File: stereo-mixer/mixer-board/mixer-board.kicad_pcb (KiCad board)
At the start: 2 copper layers, 26 parts, among them J1 Conn_01x36_Male, J2 Conn_01x03_Male

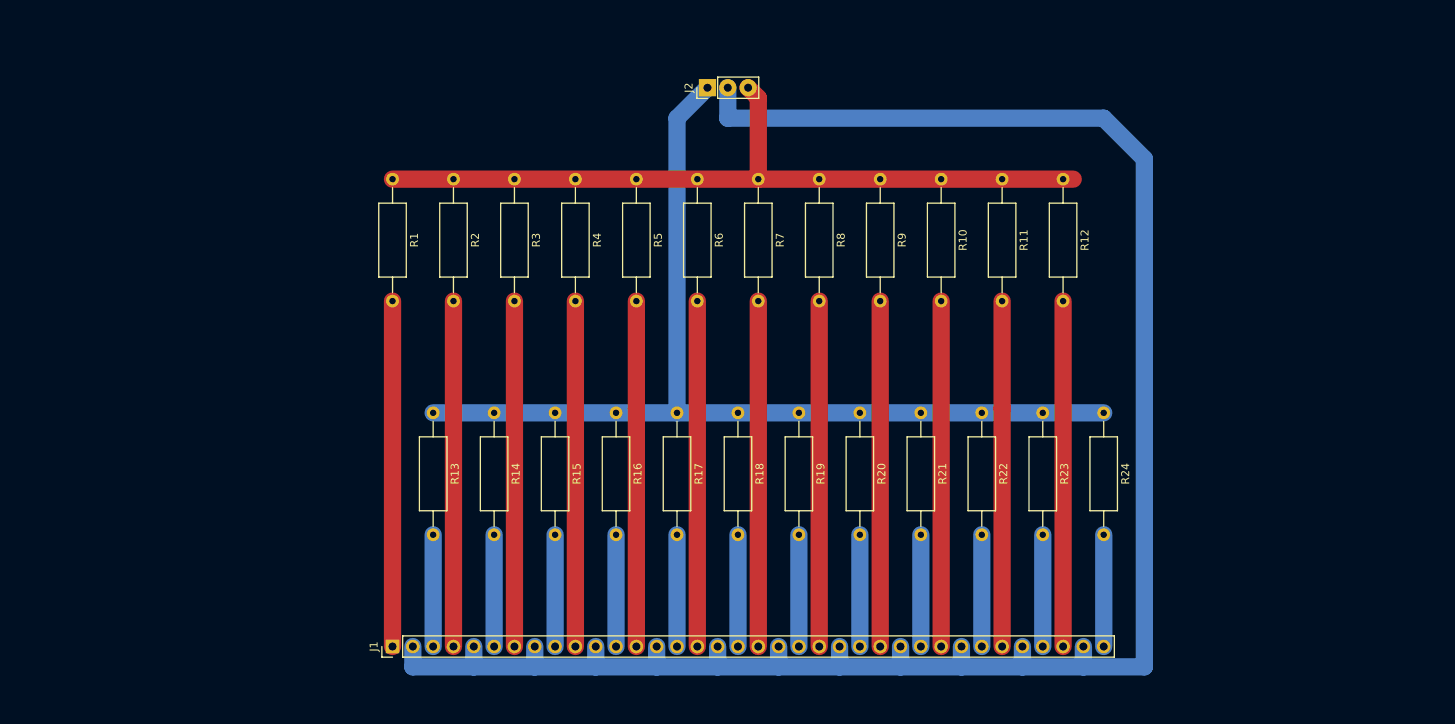
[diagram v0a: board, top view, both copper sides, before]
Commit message: added coupling caps to mixer board
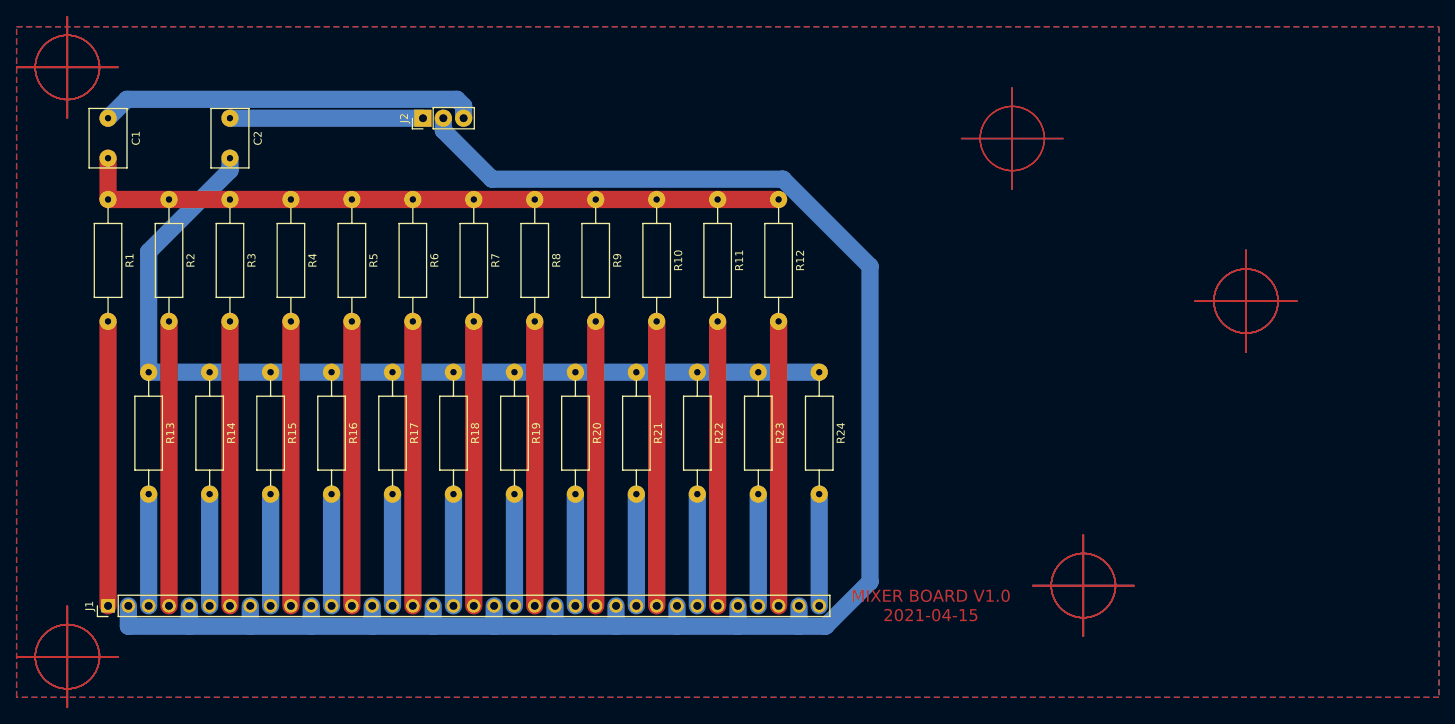
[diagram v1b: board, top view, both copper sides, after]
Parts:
- added C1: 10uF, Capacitor_THT:C_Rect_L7.2mm_W4.5mm_P5.00mm_FKS2_FKP2_MKS2_MKP2, F.Cu at (66.0, 48.3)
- added C2: 10uF, Capacitor_THT:C_Rect_L7.2mm_W4.5mm_P5.00mm_FKS2_FKP2_MKS2_MKP2, F.Cu at (81.3, 48.3)
- moved R20 35.9 mm to (124.5, 80.0)
- moved R13 35.9 mm to (71.1, 80.0)
- moved R14 35.9 mm to (78.7, 80.0)
- moved R15 35.9 mm to (86.4, 80.0)
- moved R17 35.9 mm to (101.6, 80.0)
- moved R18 35.9 mm to (109.2, 80.0)
- moved R19 35.9 mm to (116.8, 80.0)
- moved R22 35.9 mm to (139.7, 80.0)
- moved R23 35.9 mm to (147.3, 80.0)
- moved R24 35.9 mm to (154.9, 80.0)
- moved J1 35.9 mm to (66.0, 109.2)
- moved R16 35.9 mm to (94.0, 80.0)
- moved R21 35.9 mm to (132.1, 80.0)
- moved J2 35.8 mm to (105.4, 48.3)
- moved R5 35.7 mm to (96.5, 58.4)
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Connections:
- J2 pad 1: Net-(J2-Pad1) -> Net-(C2-Pad1)
- J2 pad 3: Net-(J2-Pad3) -> Net-(C1-Pad1)
- R1 pad 1: Net-(J2-Pad3) -> Net-(C1-Pad2)
- R10 pad 1: Net-(J2-Pad3) -> Net-(C1-Pad2)
- R11 pad 1: Net-(J2-Pad3) -> Net-(C1-Pad2)
- R12 pad 1: Net-(J2-Pad3) -> Net-(C1-Pad2)
- R13 pad 1: Net-(J2-Pad1) -> Net-(C2-Pad2)
- R14 pad 1: Net-(J2-Pad1) -> Net-(C2-Pad2)
- R15 pad 1: Net-(J2-Pad1) -> Net-(C2-Pad2)
- R16 pad 1: Net-(J2-Pad1) -> Net-(C2-Pad2)
- R17 pad 1: Net-(J2-Pad1) -> Net-(C2-Pad2)
- R18 pad 1: Net-(J2-Pad1) -> Net-(C2-Pad2)
- R19 pad 1: Net-(J2-Pad1) -> Net-(C2-Pad2)
- R2 pad 1: Net-(J2-Pad3) -> Net-(C1-Pad2)
- R20 pad 1: Net-(J2-Pad1) -> Net-(C2-Pad2)
- R21 pad 1: Net-(J2-Pad1) -> Net-(C2-Pad2)
- R22 pad 1: Net-(J2-Pad1) -> Net-(C2-Pad2)
- R23 pad 1: Net-(J2-Pad1) -> Net-(C2-Pad2)
- R24 pad 1: Net-(J2-Pad1) -> Net-(C2-Pad2)
- R3 pad 1: Net-(J2-Pad3) -> Net-(C1-Pad2)
- R4 pad 1: Net-(J2-Pad3) -> Net-(C1-Pad2)
- R5 pad 1: Net-(J2-Pad3) -> Net-(C1-Pad2)
- R6 pad 1: Net-(J2-Pad3) -> Net-(C1-Pad2)
- R7 pad 1: Net-(J2-Pad3) -> Net-(C1-Pad2)
- R8 pad 1: Net-(J2-Pad3) -> Net-(C1-Pad2)
- R9 pad 1: Net-(J2-Pad3) -> Net-(C1-Pad2)
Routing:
- net Net-(J2-Pad1): track 126.0 -> 0.00 mm
- net Net-(C2-Pad2): track 0.00 -> 114.8 mm
- net Net-(J2-Pad3): track 97.0 -> 0.00 mm
- net Net-(C1-Pad2): track 0.00 -> 89.0 mm
- net Net-(C1-Pad1): track 0.00 -> 47.3 mm
- net Net-(C2-Pad1): track 0.00 -> 24.1 mm
- net GND: track 243.4 -> 226.8 mm
- net Net-(J1-Pad7): track 43.2 -> 35.6 mm
- net Net-(J1-Pad4): track 43.2 -> 35.6 mm
- net Net-(J1-Pad34): track 43.2 -> 35.6 mm
- net Net-(J1-Pad31): track 43.2 -> 35.6 mm
- net Net-(J1-Pad28): track 43.2 -> 35.6 mm
- net Net-(J1-Pad25): track 43.2 -> 35.6 mm
- net Net-(J1-Pad22): track 43.2 -> 35.6 mm
- net Net-(J1-Pad19): track 43.2 -> 35.6 mm
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- added copper zone on B.Cu, net (none)
- added copper zone on F.Cu, net (none)
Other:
- board text added: "MIXER BOARD V1.0 2021-04-15"
